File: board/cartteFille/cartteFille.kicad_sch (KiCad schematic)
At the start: 57 parts, among them U11 MAX4040EUKT, U20 MCP23018-E/SS, U21-2 SN74LVC2G14DBVTG4, U23-4 SN74LVC2G14DBVTG4, U25-6 SN74LVC2G14DBVTG4, U27-8 SN74LVC2G14DBVTG4

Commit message: backup avant rajout du driver led
pour avoir la version sans driver led
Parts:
- removed S21, S22, S23, S24: 3-2213818-2, 3-2213818-2:SW_3-2213818-2, symbol 3-2213818-2:3-2213818-2
- added S21, S22, S23, S24: 3006.2100, 3006:3006.2100, symbol 3006.2100:3006.2100
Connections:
- net GND: now also S21.1, S22.1, S23.1, S24.1
- net U20GPB3-U278S28: now reaches U20.5 (GPB3), U27-8.4 (2Y)
- net U20GPB2-U278S27: now reaches U20.4 (GPB2), U27-8.6 (1Y)
- net at R211.2, R212.1: now also S21.2
- net U20GPA4-S21LED: now reaches U20.21 (GPA4)
- net U20GPA4-S21LED: now also S21.K
- net at R213.1: now also S21.A
- net U20GPB1-U256S26: now reaches U20.3 (GPB1), U25-6.4 (2Y)
- net U20GPB0-U256S25: now reaches U20.2 (GPB0), U25-6.6 (1Y)
- net ADC_CH0-U11RP1: now reaches C11.1, EXT2.2, R12.1
- net at R223.1: now also S22.A
- net at R241.2, R242.1: now also S24.2
- net U20GPA7-S24LED: now reaches U20.24 (GPA7)
- net U20GPA7-S24LED: now also S24.K
- net at R243.1: now also S24.A
- net U20GPA2-S27LED: now reaches S27.K, U20.19 (GPA2)
- net GPIO3-U20RESET: now reaches EXT1.8, U20.14 (~{RESET})
- net U20GPA3-S28LED: now reaches S28.K, U20.20 (GPA3)
- net I2C_SCL: now reaches EXT2.7, U20.11 (SCL)
- net I2C_SDA: now reaches EXT2.10, U20.12 (SDA)
- net GPIO32-INTB: now reaches U20.15 (INTB)
- net GPIO32-INTB: now also EXT2.6; no longer EXT2.5
- net GPIO33-INTA: now reaches U20.16 (INTA)
- net GPIO33-INTA: now also EXT2.5; no longer EXT2.6
- net U20GPA0-S25LED: now reaches S25.K, U20.17 (GPA0)
- net U20GPA1-S26LED: now reaches S26.K, U20.18 (GPA1)
- net U20GPA5-S22LED: now reaches U20.22 (GPA5)
- net U20GPA5-S22LED: now also S22.K
- net U20GPA6-S23LED: now reaches U20.23 (GPA6)
- net U20GPA6-S23LED: now also S23.K
- net U20GPB4-U212S21: now reaches U20.6 (GPB4), U21-2.6 (1Y)
- net U20GPB5-U212S22: now reaches U20.7 (GPB5), U21-2.4 (2Y)
- net U20GPB6-U234S23: now reaches U20.8 (GPB6), U23-4.6 (1Y)
- net U20GPB7-U234S24: now reaches U20.9 (GPB7), U23-4.4 (2Y)
- net at R233.1: now also S23.A
- net at R221.2, R222.1: now also S22.2
- net at R231.2, R232.1: now also S23.2
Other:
- note added: "Buttons"
- note added: "ESP32 IN/OUT"
- note added: "GPIO"
- note added: "Potentiometer"
- moved on the sheet: C11, C12, C211, C221, C231, C241, C251, C261, C271, C281, EXT1, EXT2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

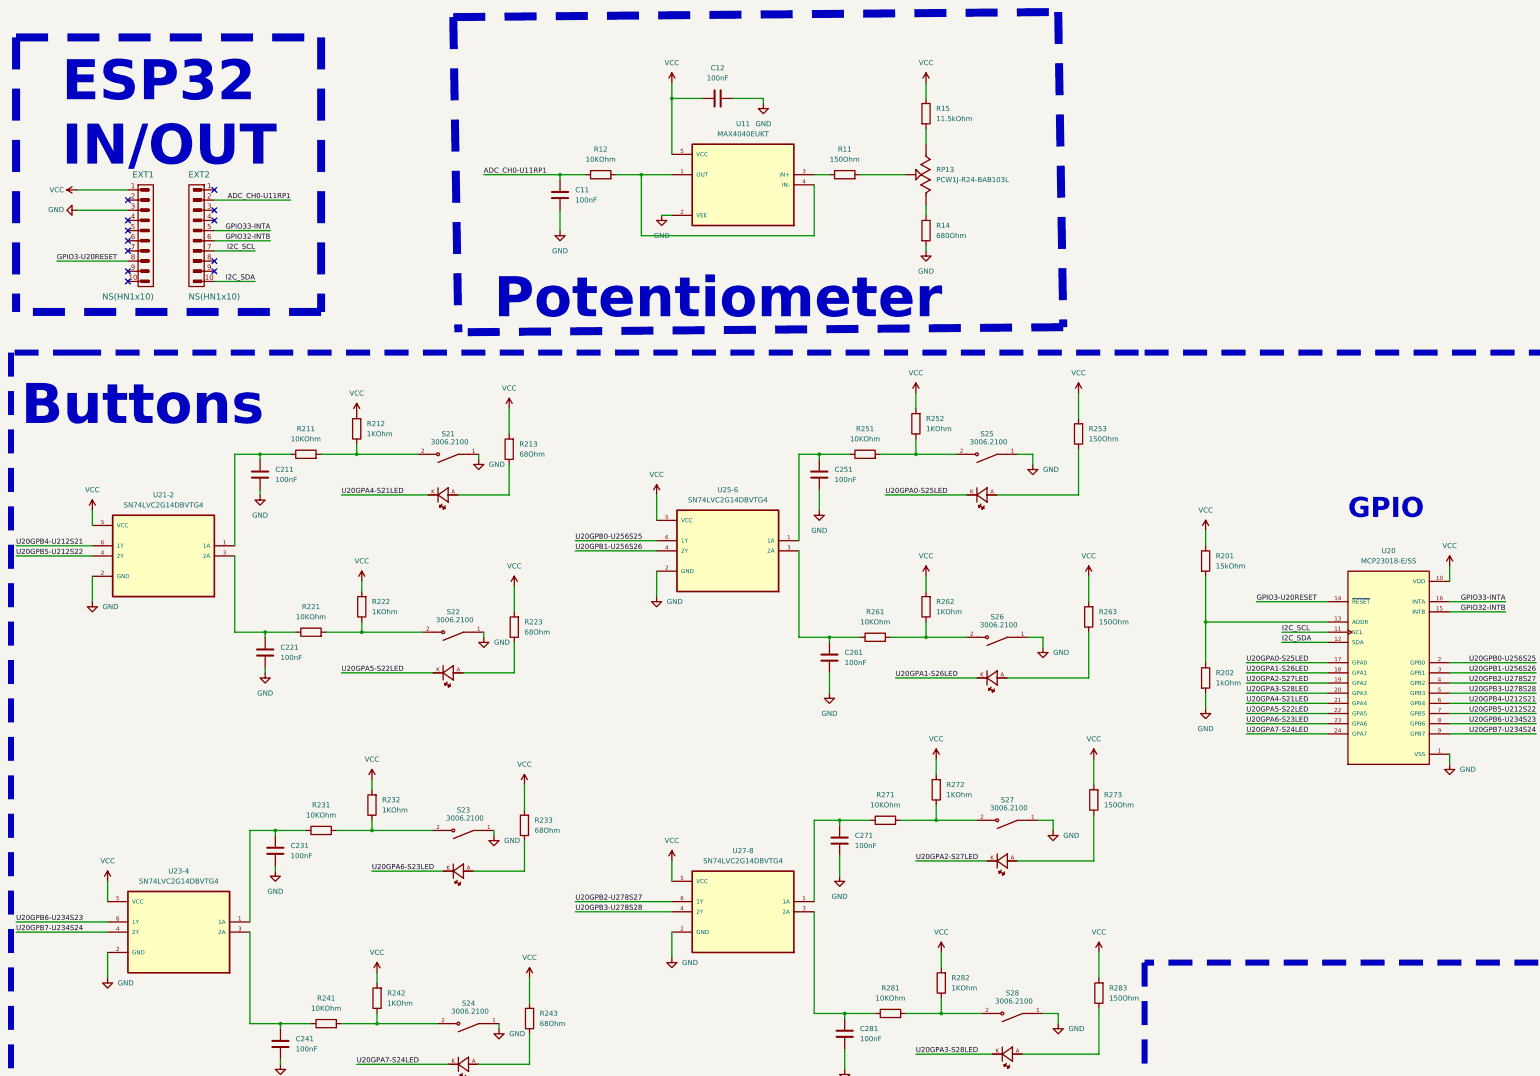
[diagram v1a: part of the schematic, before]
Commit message: 5V_to_3.3V
Changement générale de tension du 5v au 3.3v
tous les composant peuvent travailler sous les 2 tension les calcules de résistance... on été refais /cherché dans la doc... étonnement peux de changement ont été nécessaires
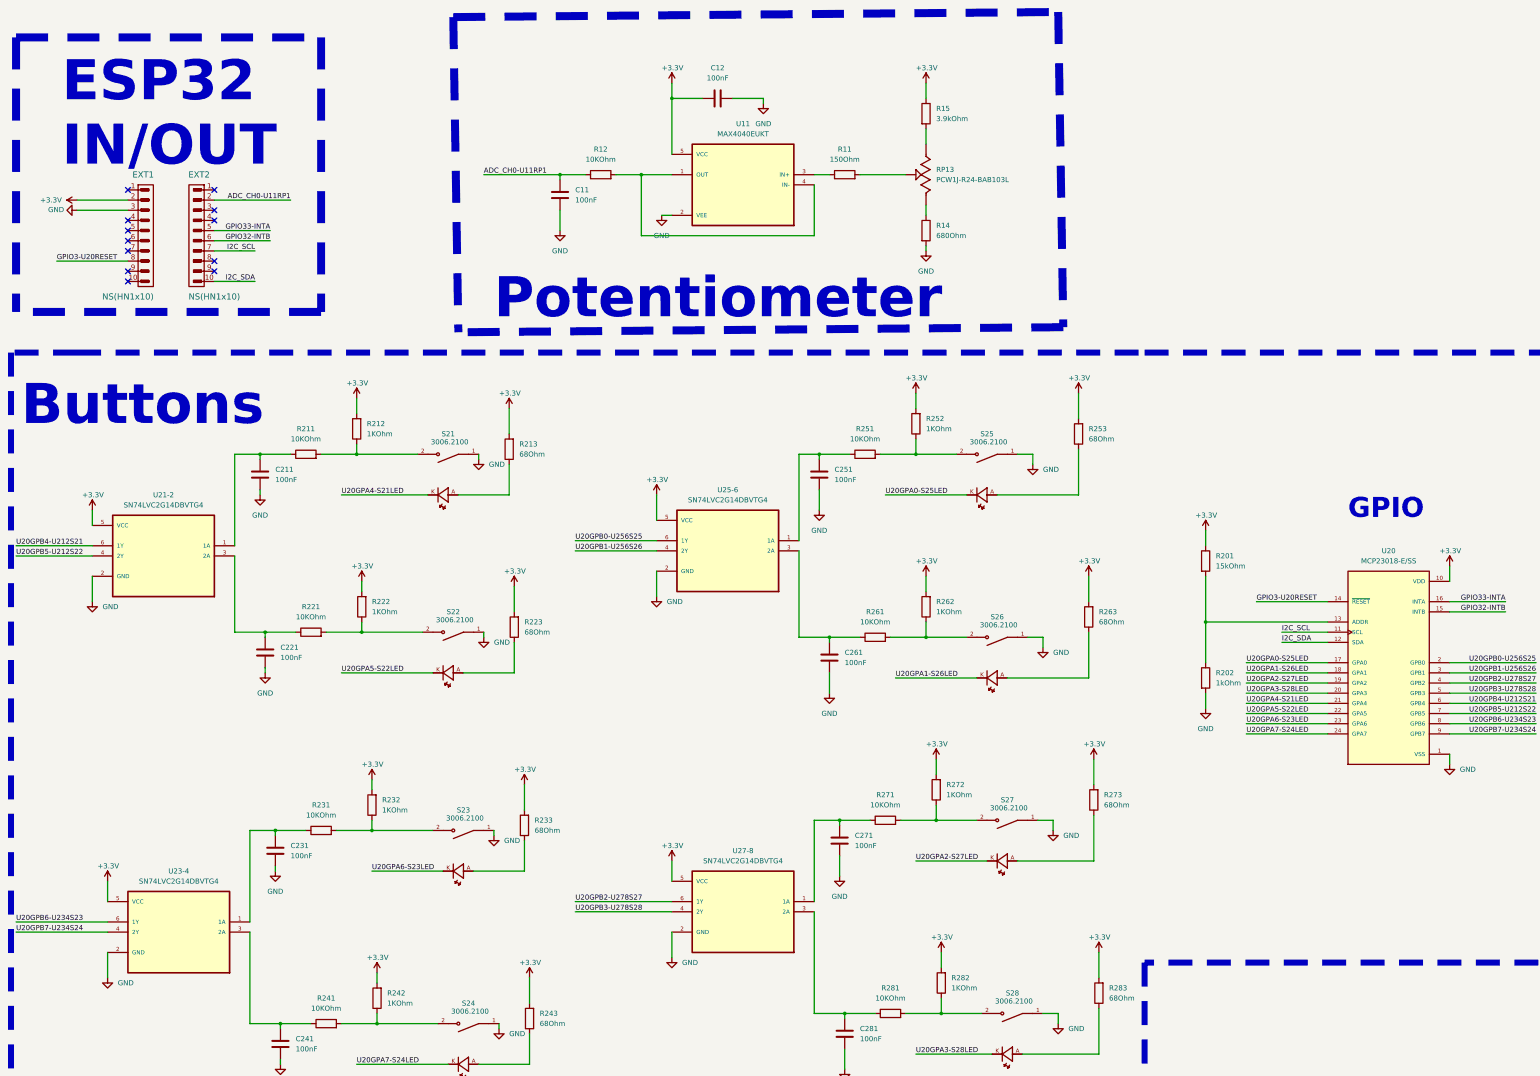
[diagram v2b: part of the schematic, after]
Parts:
- R15: value 11.5kOhm -> 3.9kOhm
- R253, R263, R273, R283: value 150Ohm -> 68Ohm
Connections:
- net +3V3: now reaches EXT1.2
- net +3V3: now also C12.1, R15.1, R201.1, R212.2, R213.2, R222.2, R223.2, R232.2, R233.2, R242.2, R243.2, R252.2, R253.2, R262.2, R263.2, R272.2, R273.2, R282.2, R283.2, U11.5 (VCC), U20.10 (VDD), U21-2.5 (VCC), U23-4.5 (VCC), U25-6.5 (VCC), U27-8.5 (VCC)
- removed net VCC: C12.1, EXT1.1, R15.1, R201.1, R212.2, R213.2, R222.2, R223.2, R232.2, R233.2, R242.2, R243.2, R252.2, R253.2, R262.2, R263.2, R272.2, R273.2, R282.2, R283.2, U11.5 (VCC), U20.10 (VDD), U21-2.5 (VCC), U23-4.5 (VCC), U25-6.5 (VCC), U27-8.5 (VCC)

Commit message: end_sch
fin du schéma électrique début du pcb
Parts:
- added D21, D22, D23, D24, D25, D26, D27, D28: NSI45020T1G, NSI45020T1G:SOD3716X135N, symbol NSI45020T1G:NSI45020T1G
- EXT1, EXT2: footprint OLIMEX_Connectors-FP:HN1x10 -> connecteur:HN1x10
- R213, R223, R233, R243, R253, R263, R273, R283: value 68Ohm -> 150Ohm
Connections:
- net +3V3: no longer R213.2, R223.2, R233.2, R243.2, R253.2, R263.2, R273.2, R283.2
- net at R223.1, S22.A: now also D22.1
- net at R263.1, S26.A: now also D26.1
- net at R283.1, S28.A: now also D28.1
- net at R213.1, S21.A: now also D21.1
- net at R243.1, S24.A: now also D24.1
- net at R273.1, S27.A: now also D27.1
- net +5V: now reaches EXT1.1
- net +5V: now also R213.2, R223.2, R233.2, R243.2, R253.2, R263.2, R273.2, R283.2, D21.2, D22.2, D23.2, D24.2, D25.2, D26.2, D27.2, D28.2
- net at R233.1, S23.A: now also D23.1
- net at R253.1, S25.A: now also D25.1
- no-connect marks 12 -> 11
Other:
- note added: "1-Resistor"
- note added: "2-Current Regulator"
- note added: "GPIO LED&BUTTON"
- note added: "ILED driver either 1 or 2:"
- note added: "Op-amp Buffer"
- note added: "Potentiometer coupling 0.15-2.45V"
- note added: "RC Filter"
- note added: "Resitors for I2C adresse 0x00000000"
- note added: "S21 Button"
- note added: "S22 Button"
- note added: "S23 Button"
- note added: "S24 Button"
- note added: "S25 Button"
- note added: "S26 Button"
- note added: "S27 Button"
- note added: "S28 Button"
- note removed: "GPIO"
- company: (none) -> Help-Tec Automation
- title: (none) -> Peripheral Board
- moved on the sheet: C11, C12, C211, C221, C231, C241, C251, C261, C271, C281, R11, R12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

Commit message: push sous schémat
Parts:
- removed C211, C221, C231, C241, C251, C261, C271, C281: 100nF, Capacitor_SMD:C_0603_1608Metric, symbol Device:C
- removed D21, D22, D23, D24, D25, D26, D27, D28: NSI45020T1G, NSI45020T1G:SOD3716X135N, symbol NSI45020T1G:NSI45020T1G
- removed R211, R221, R231, R241, R251, R261, R271, R281: 10KOhm, Resistor_SMD:R_0603_1608Metric, symbol Device:R
- removed R212, R222, R232, R242, R252, R262, R272, R282: 1KOhm, Resistor_SMD:R_0603_1608Metric, symbol Device:R
- removed R213, R223, R233, R243, R253, R263, R273, R283: 150Ohm, Resistor_SMD:R_0603_1608Metric, symbol Device:R
- removed S21, S22, S23, S24, S25, S26, S27, S28: 3006.2100, 3006:3006.2100, symbol 3006.2100:3006.2100
- removed U21-2, U23-4, U25-6, U27-8: SN74LVC2G14DBVTG4, SN74LVC2G14DBVTG4:SOT95P280X145-6N, symbol SN74LVC2G14DBVTG4:SN74LVC2G14DBVTG4
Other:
- added sheet ButtonS21-S22_Sheet (button.kicad_sch)
- added sheet ButtonS23-S24_Sheet (button.kicad_sch)
- added sheet ButtonS25-S26_Sheet (button.kicad_sch)
- added sheet ButtonS27-S28_Sheet (button.kicad_sch)
- note removed: "1-Resistor"
- note removed: "2-Current Regulator"
- note removed: "ILED driver either 1 or 2:"
- note removed: "S21 Button"
- note removed: "S22 Button"
- note removed: "S23 Button"
- note removed: "S24 Button"
- note removed: "S25 Button"
- note removed: "S26 Button"
- note removed: "S27 Button"
- note removed: "S28 Button"
- moved on the sheet: R201, R202, U20

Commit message: end of the day
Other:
- note added: "RC Filter fc ~160Hz"
- note removed: "RC Filter"
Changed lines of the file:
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@@
     (stroke (width 0) (type default) (color 0 0 0 0))
   )
-  (polyline (pts (xy 93.98 13.97) (xy 232.41 13.97))
-    (stroke (width 1.5) (type dash_dot) (color 0 0 0 0))
-  )
-  (polyline (pts (xy 232.41 13.97) (xy 232.41 86.36))
+  (polyline (pts (xy 93.98 13.97) (xy 238.76 13.97))
+    (stroke (width 1.5) (type dash_dot) (color 0 0 0 0))
+  )
+  (polyline (pts (xy 238.76 13.97) (xy 238.76 86.36))
     (stroke (width 1.5) (type dash_dot) (color 0 0 0 0))
   )
@@
     (stroke (width 0) (type default) (color 0 0 0 0))
   )
-  (polyline (pts (xy 232.41 86.36) (xy 93.98 86.36))
+  (polyline (pts (xy 238.76 86.36) (xy 93.98 86.36))
     (stroke (width 1.5) (type dash_dot) (color 0 0 0 0))
   )
@@
     (effects (font (size 1.5 1.5) (thickness 0.3) bold italic) (justify left bottom))
   )
+  (text "RC Filter\nfc ~160Hz" (at 110.49 39.37 0)
+    (effects (font (size 1.5 1.5) (thickness 0.3) bold italic) (justify left bottom))
+  )
   (text "Op-amp\nBuffer" (at 163.83 24.13 0)
     (effects (font (size 1.5 1.5) (thickness 0.3) bold italic) (justify left bottom))
@@
     (effects (font (size 6 6) (thickness 2) bold) (justify left bottom))
   )
-  (text "RC Filter" (at 115.57 36.83 0)
-    (effects (font (size 1.5 1.5) (thickness 0.3) bold italic) (justify left bottom))
-  )
   (text "GPIO LED&BUTTON" (at 92.71 128.27 0)
